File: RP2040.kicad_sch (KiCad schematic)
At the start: 19 parts, among them U3 RP2040, Y1 12MHz

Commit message: Final refinements before issue to JLC
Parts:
- added J1: Conn_01x02_Male, Connector_PinHeader_2.54mm:PinHeader_1x02_P2.54mm_Vertical, symbol Connector:Conn_01x02_Male
- added TP5, TP6, TP7: TestPoint_Flag, TestPoint:TestPoint_Pad_D1.5mm, symbol Connector:TestPoint_Flag
- renumbered C13 to C1, C7 to C10, C3 to C11, C9 to C2, C10 to C3, C15 to C4, C14 to C5, C8 to C6, C17 to C7, C12 to C8, C6 to C9, R7 to R3, R8 to R4, R4 to R5, R11 to R6, U3 to U1
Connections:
- net at U1.38 (GPIO26_ADC0): now also TP5.1
- net at U1.39 (GPIO27_ADC1): now also TP6.1
- net at U1.40 (GPIO28_ADC2): now also TP7.1
- net SWCLK: no longer names the net of U1.24 (SWCLK)
- net SWCLK: now also J1.1 (Pin_1)
- net SWD: no longer names the net of U1.25 (SWD)
- net SWD: now also J1.2 (Pin_2)
- no-connect marks 6 -> 3

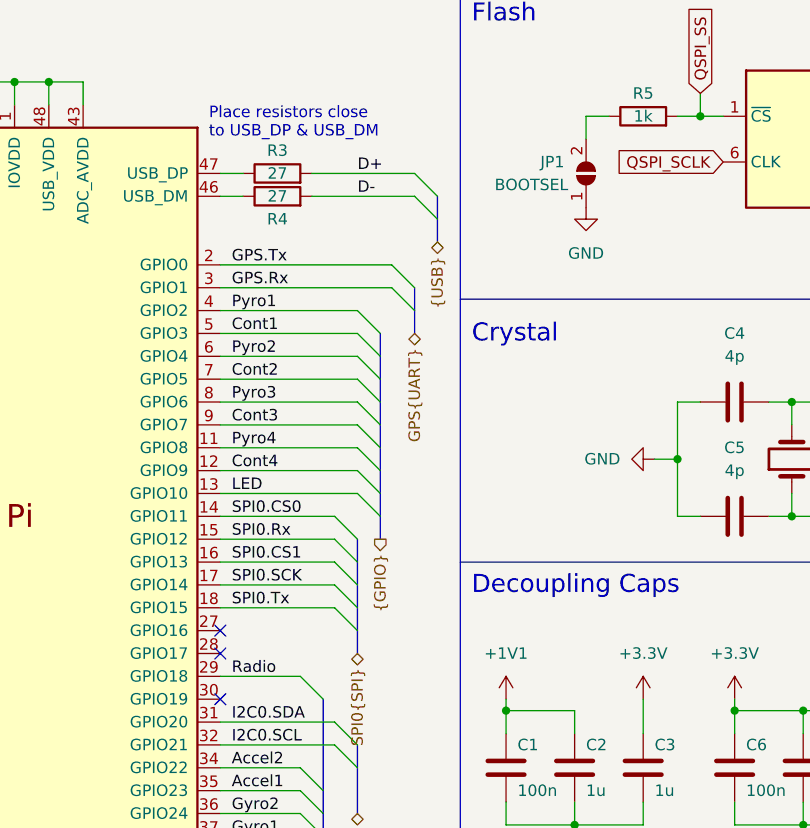
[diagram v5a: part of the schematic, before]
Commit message: rev2 changes excluding pyro
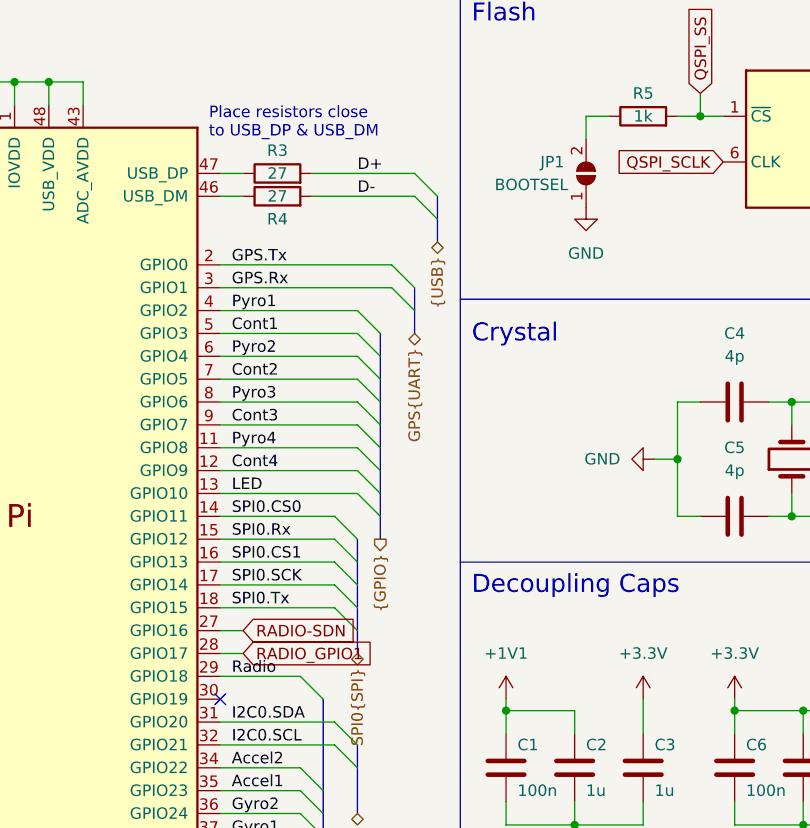
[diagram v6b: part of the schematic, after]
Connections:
- net RADIO-SDN: now reaches U1.27 (GPIO16)
- net RADIO_GPIO1: now reaches U1.28 (GPIO17)
- no-connect marks 3 -> 1
